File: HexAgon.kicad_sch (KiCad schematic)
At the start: 0 parts

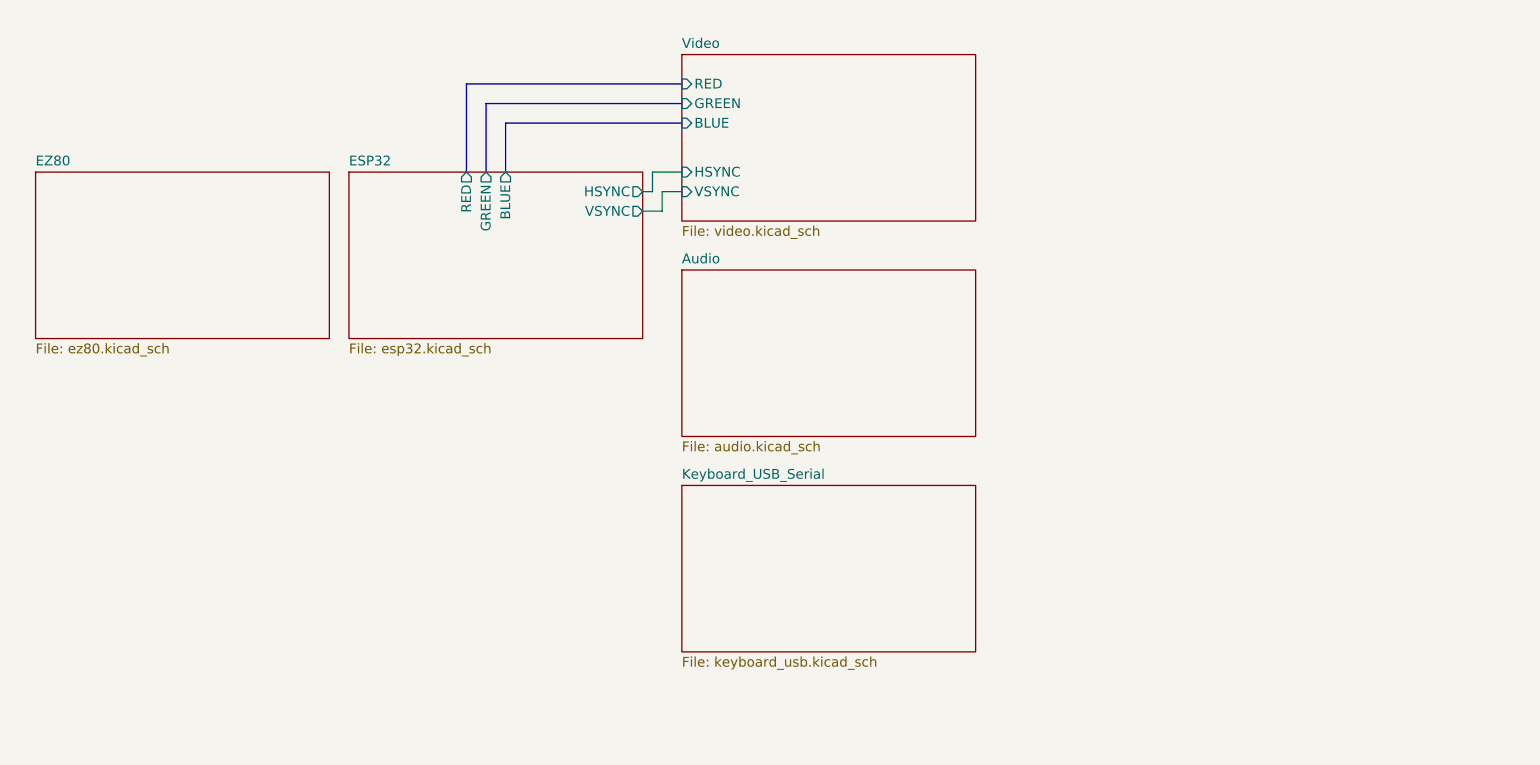
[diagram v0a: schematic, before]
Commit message: schematics finished, pcb routing 80%
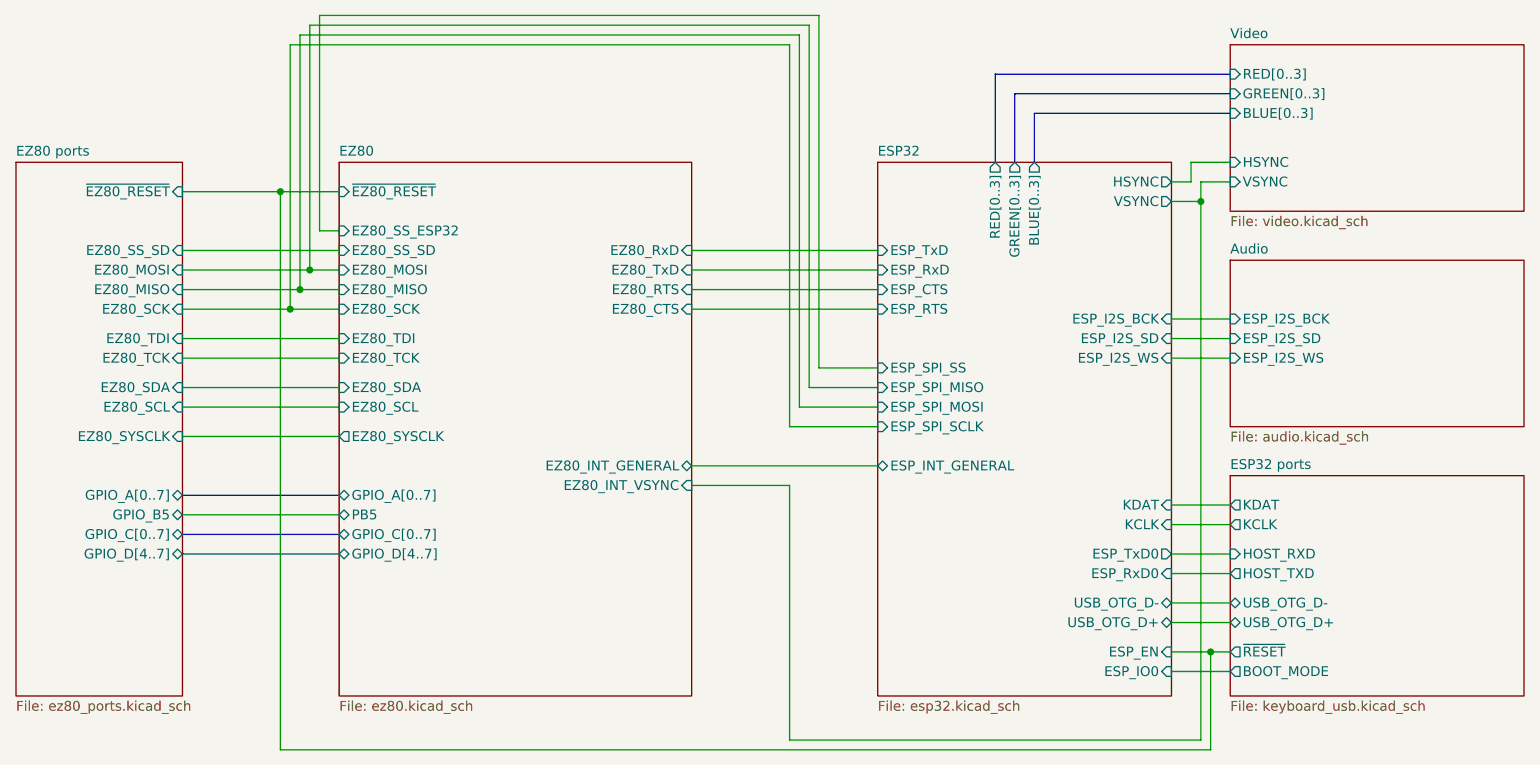
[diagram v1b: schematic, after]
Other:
- sheet Keyboard_USB_Serial renamed ESP32 ports
- added sheet EZ80 ports (ez80_ports.kicad_sch)
- sheet Audio ports: added ESP_I2S_BCK, ESP_I2S_SD, ESP_I2S_WS; removed none
- sheet ESP32 ports: added BLUE[0..3], ESP_CTS, ESP_EN, ESP_I2S_BCK, ESP_I2S_SD, ESP_I2S_WS, ESP_INT_GENERAL, ESP_IO0, ESP_RTS, ESP_RxD, ESP_RxD0, ESP_SPI_MISO, ESP_SPI_MOSI, ESP_SPI_SCLK, ESP_SPI_SS, ESP_TxD, ESP_TxD0, GREEN[0..3], KCLK, KDAT, RED[0..3], USB_OTG_D+, USB_OTG_D-; removed BLUE, GREEN, RED
- sheet ESP32 ports ports: added BOOT_MODE, HOST_RXD, HOST_TXD, KCLK, KDAT, USB_OTG_D+, USB_OTG_D-, ~{RESET}; removed none
- sheet EZ80 ports: added EZ80_CTS, EZ80_INT_GENERAL, EZ80_INT_VSYNC, EZ80_MISO, EZ80_MOSI, EZ80_RTS, EZ80_RxD, EZ80_SCK, EZ80_SCL, EZ80_SDA, EZ80_SS_ESP32, EZ80_SS_SD, EZ80_SYSCLK, EZ80_TCK, EZ80_TDI, EZ80_TxD, GPIO_A[0..7], GPIO_C[0..7], GPIO_D[4..7], PB5, ~{EZ80_RESET}; removed none
- sheet Video ports: added BLUE[0..3], GREEN[0..3], RED[0..3]; removed BLUE, GREEN, RED

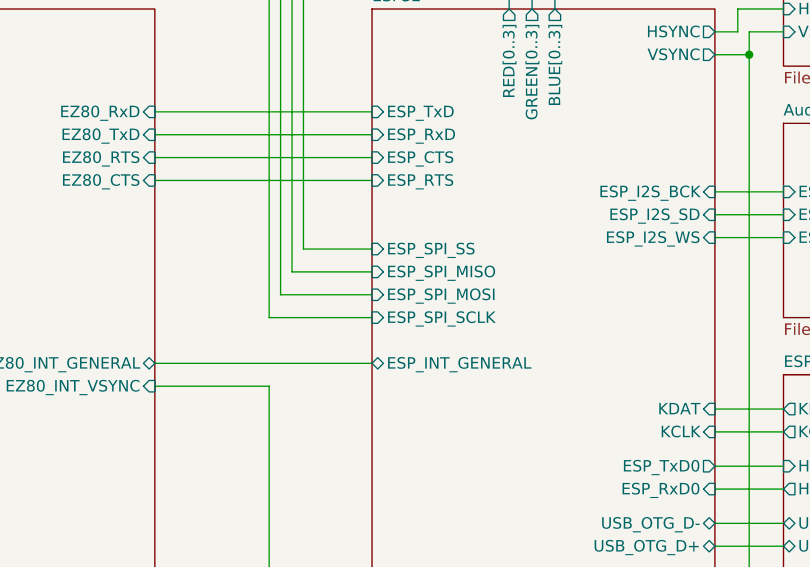
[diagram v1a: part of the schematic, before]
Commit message: fixed SD card issues
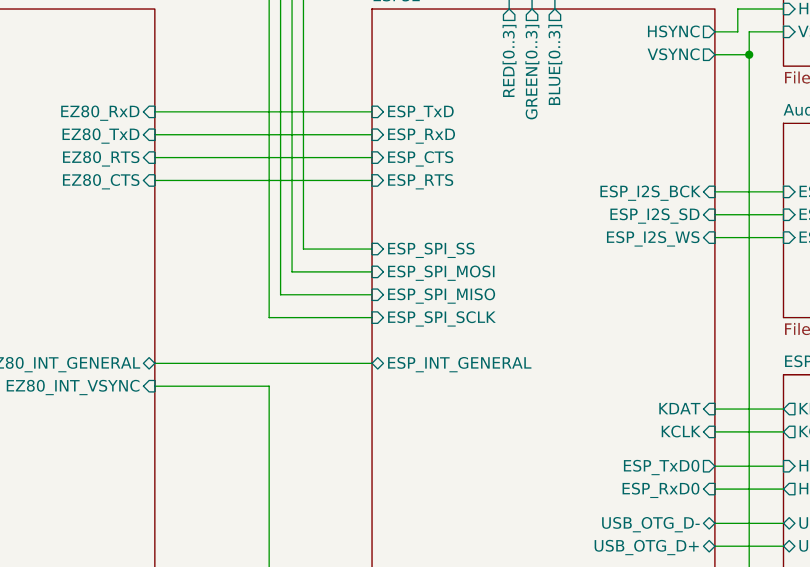
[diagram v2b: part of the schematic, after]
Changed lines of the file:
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@@
 	(wire
 		(pts
-			(xy 170.18 101.6) (xy 160.02 101.6)
+			(xy 161.29 99.06) (xy 170.18 99.06)
 		)
 		(stroke
@@
 	(wire
 		(pts
-			(xy 170.18 99.06) (xy 161.29 99.06)
-		)
-		(stroke
-			(width 0)
-			(type default)
-		)
-	)
-	(wire
-		(pts
 			(xy 80.01 101.6) (xy 100.33 101.6)
 		)
@@
 		(pts
 			(xy 80.01 83.82) (xy 96.52 83.82)
+		)
+		(stroke
+			(width 0)
+			(type default)
+		)
+	)
+	(wire
+		(pts
+			(xy 160.02 101.6) (xy 170.18 101.6)
 		)
 		(stroke
@@
 		)
 		(pin "ESP_SPI_MOSI" input
+			(at 170.18 99.06 180)
+			(effects
+				(font
+					(size 1.27 1.27)
+				)
+				(justify left)
+			)
+		)
+		(pin "ESP_SPI_MISO" input
 			(at 170.18 101.6 180)
 			(effects
 				(font
-					(size 1.27 1.27)
-				)
-				(justify left)
-			)
-		)
-		(pin "ESP_SPI_MISO" input
-			(at 170.18 99.06 180)
-			(effects
-				(font
